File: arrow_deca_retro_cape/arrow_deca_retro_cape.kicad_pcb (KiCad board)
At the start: 4 copper layers, 73.7 x 62 mm, 23 parts, among them J1 PMOD_A, J2 P8_Male, J3 P9_Male, U1 AS4C32M16SB-7TIN, U2 AS4C32M16SB-7TIN, U3 74LVC1G04

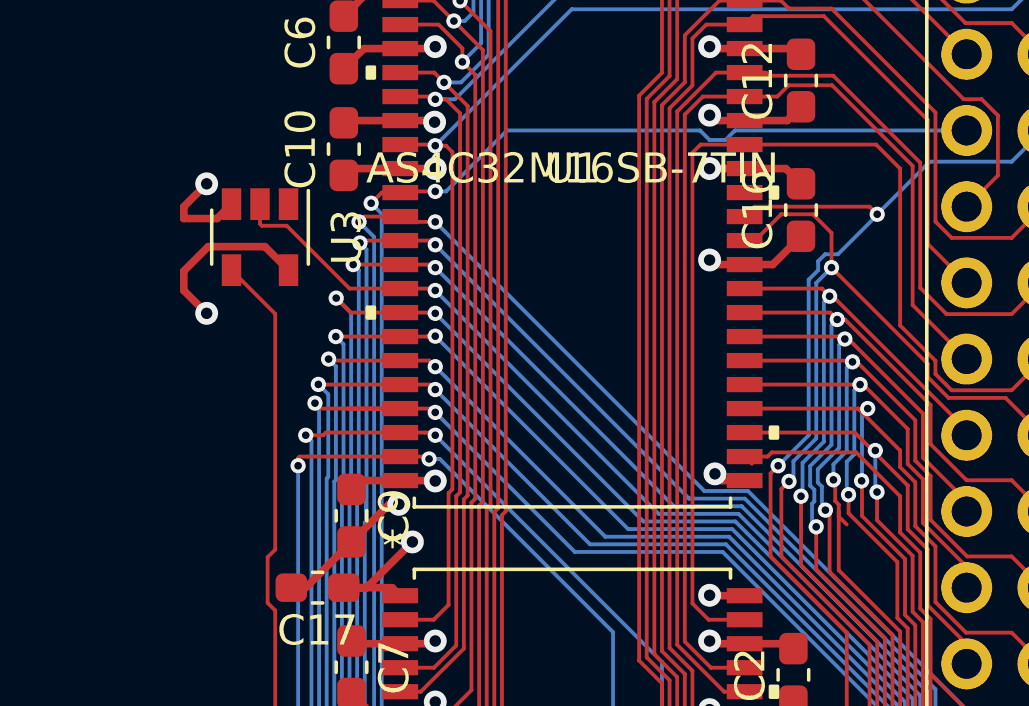
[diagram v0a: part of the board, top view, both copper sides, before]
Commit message: Starting to add VGA.
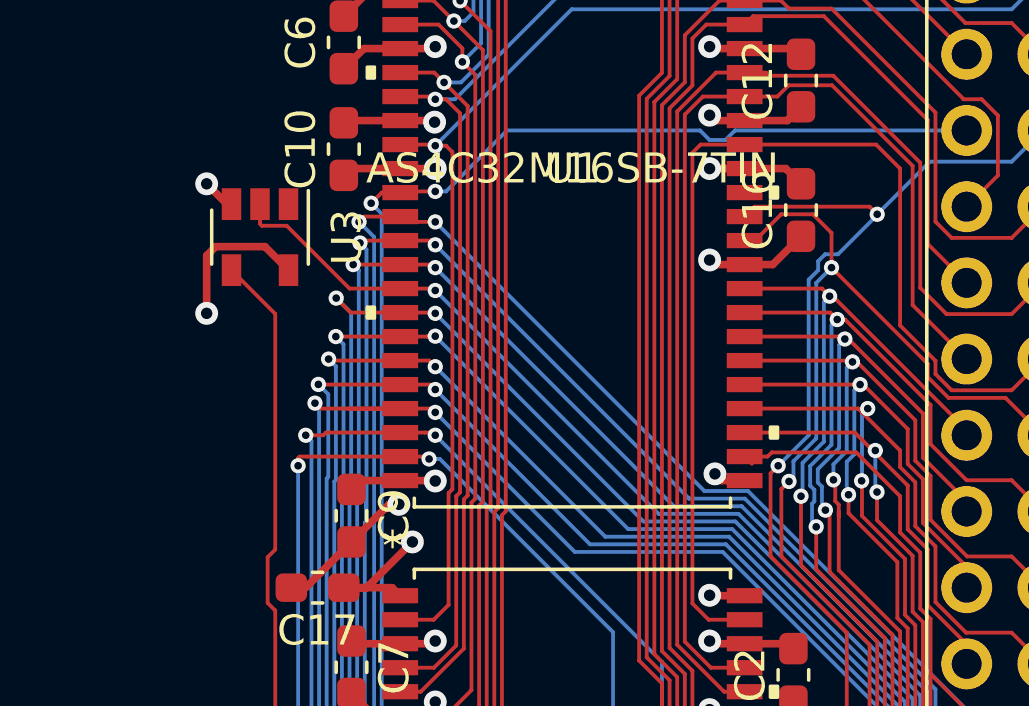
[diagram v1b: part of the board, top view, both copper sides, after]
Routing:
- net GND: track 340.9 -> 338.8 mm
- net +3V3: track 258.1 -> 257.3 mm
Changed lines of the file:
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@@
     (thickness 1.6)
     (drawings 4)
-    (tracks 1069)
+    (tracks 1065)
     (zones 0)
     (modules 23)
@@
   (segment (start 109.474 46.736) (end 109.474 55.626) (width 0.254) (layer In1.Cu) (net 1))
   (segment (start 109.474 55.626) (end 109.474 59.436) (width 0.254) (layer In1.Cu) (net 1))
-  (segment (start 96.615 48.655) (end 97.094 48.176) (width 0.254) (layer F.Cu) (net 1))
-  (segment (start 95.504 48.655) (end 96.615 48.655) (width 0.254) (layer F.Cu) (net 1))
-  (segment (start 95.504 48.26) (end 96.266 47.498) (width 0.254) (layer F.Cu) (net 1))
   (via (at 96.266 47.498) (size 0.762) (drill 0.381) (layers F.Cu B.Cu) (net 1))
-  (segment (start 95.504 48.655) (end 95.504 48.26) (width 0.254) (layer F.Cu) (net 1))
   (segment (start 109.474 46.228) (end 107.696 46.228) (width 0.254) (layer In1.Cu) (net 1))
   (segment (start 109.474 44.704) (end 109.474 46.228) (width 0.254) (layer In1.Cu) (net 1))
@@
   (segment (start 110.998 65.278) (end 110.49 64.77) (width 0.254) (layer In1.Cu) (net 1))
   (segment (start 109.474 64.77) (end 110.49 64.77) (width 0.254) (layer In1.Cu) (net 1))
+  (segment (start 96.944 48.176) (end 96.266 47.498) (width 0.254) (layer F.Cu) (net 1))
+  (segment (start 97.094 48.176) (end 96.944 48.176) (width 0.254) (layer F.Cu) (net 1))
   (segment (start 65.999557 44.679499) (end 60.706 39.385942) (width 0.127) (layer F.Cu) (net 17))
   (segment (start 67.539499 44.679499) (end 65.999557 44.679499) (width 0.127) (layer F.Cu) (net 17))
@@
   (segment (start 105.156 27.94) (end 108.712 31.496) (width 0.254) (layer In2.Cu) (net 26))
   (segment (start 102.7176 57.39) (end 101.388 57.39) (width 0.254) (layer F.Cu) (net 26))
-  (segment (start 98.209999 49.591999) (end 96.317001 49.591999) (width 0.254) (layer F.Cu) (net 26))
-  (segment (start 96.317001 49.591999) (end 95.504 50.405) (width 0.254) (layer F.Cu) (net 26))
-  (segment (start 98.994 50.376) (end 98.209999 49.591999) (width 0.254) (layer F.Cu) (net 26))
   (via (at 96.266 51.816) (size 0.762) (drill 0.381) (layers F.Cu B.Cu) (net 26))
-  (segment (start 95.504 51.054) (end 96.266 51.816) (width 0.254) (layer F.Cu) (net 26))
-  (segment (start 95.504 50.405) (end 95.504 51.054) (width 0.254) (layer F.Cu) (net 26))
   (segment (start 96.266 51.816) (end 96.266 50.038) (width 0.254) (layer In2.Cu) (net 26))
   (segment (start 99.314 46.99) (end 103.886 46.99) (width 0.254) (layer In2.Cu) (net 26))
@@
   (segment (start 105.918 59.436) (end 103.124 59.436) (width 0.254) (layer In2.Cu) (net 26))
   (segment (start 106.426 59.944) (end 105.918 59.436) (width 0.254) (layer In2.Cu) (net 26))
+  (segment (start 96.266 49.891798) (end 96.266 51.816) (width 0.254) (layer F.Cu) (net 26))
+  (segment (start 98.209999 49.591999) (end 96.565799 49.591999) (width 0.254) (layer F.Cu) (net 26))
+  (segment (start 96.565799 49.591999) (end 96.266 49.891798) (width 0.254) (layer F.Cu) (net 26))
+  (segment (start 98.994 50.376) (end 98.209999 49.591999) (width 0.254) (layer F.Cu) (net 26))
   (via (at 101.854 81.28) (size 0.508) (drill 0.254) (layers F.Cu B.Cu) (net 27))
   (segment (start 102.665599 81.28) (end 102.7176 81.227999) (width 0.127) (layer F.Cu) (net 27))
@@
   (segment (start 119.797466 61.762116) (end 119.797466 59.897015) (width 0.127) (layer F.Cu) (net 42))
   (via (at 117.158245 57.365676) (size 0.508) (drill 0.254) (layers F.Cu B.Cu) (net 43))
-  (segment (start 117.601979 58.854098) (end 117.335379 58.587498) (width 0.127) (layer F.Cu) (net 43))
   (segment (start 117.55715 75.39315) (end 117.601979 75.348321) (width 0.127) (layer F.Cu) (net 43))
   (segment (start 117.335379 58.587498) (end 117.335379 58.432621) (width 0.127) (layer F.Cu) (net 43))

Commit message: Layout finished.
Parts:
- added J4: JOY0, snapeda:TE_1-1634580-2, F.Cu at (55.2, 39.4)
- added J5: MD-60SM, MD-60SM:MD-60SM, F.Cu at (100.8, 26.4)
- added J6: JOY1, snapeda:TE_1-1634580-2, F.Cu at (55.2, 71.2)
- added R1: 1K, Resistor_SMD:R_0603_1608Metric_Pad1.05x0.95mm_HandSolder, F.Cu at (118.1, 32.9)
- added R10: 2K, Resistor_SMD:R_0603_1608Metric_Pad1.05x0.95mm_HandSolder, F.Cu at (60.4, 36.6)
- added R11: 2K, Resistor_SMD:R_0603_1608Metric_Pad1.05x0.95mm_HandSolder, F.Cu at (60.4, 33.5)
- added R12: 2K, Resistor_SMD:R_0603_1608Metric_Pad1.05x0.95mm_HandSolder, F.Cu at (60.4, 80.1)
- added R13: 2K, Resistor_SMD:R_0603_1608Metric_Pad1.05x0.95mm_HandSolder, F.Cu at (60.4, 77.1)
- added R14: 2K, Resistor_SMD:R_0603_1608Metric_Pad1.05x0.95mm_HandSolder, F.Cu at (60.4, 74.0)
- added R15: 2K, Resistor_SMD:R_0603_1608Metric_Pad1.05x0.95mm_HandSolder, F.Cu at (60.4, 71.0)
- added R16: 2K, Resistor_SMD:R_0603_1608Metric_Pad1.05x0.95mm_HandSolder, F.Cu at (60.4, 67.9)
- added R17: 2K, Resistor_SMD:R_0603_1608Metric_Pad1.05x0.95mm_HandSolder, F.Cu at (60.4, 64.9)
- added R18: 2K, Resistor_SMD:R_0603_1608Metric_Pad1.05x0.95mm_HandSolder, F.Cu at (60.4, 61.8)
- added R19: 5K, Resistor_SMD:R_0603_1608Metric_Pad1.05x0.95mm_HandSolder, F.Cu at (60.4, 50.3)
- added R2: 1K, Resistor_SMD:R_0603_1608Metric_Pad1.05x0.95mm_HandSolder, F.Cu at (118.1, 28.4)
- added R20: 5K, Resistor_SMD:R_0603_1608Metric_Pad1.05x0.95mm_HandSolder, F.Cu at (60.4, 78.6)
- added R21: 5K, Resistor_SMD:R_0603_1608Metric_Pad1.05x0.95mm_HandSolder, F.Cu at (60.4, 47.2)
- added R22: 5K, Resistor_SMD:R_0603_1608Metric_Pad1.05x0.95mm_HandSolder, F.Cu at (60.4, 75.6)
- added R23: 5K, Resistor_SMD:R_0603_1608Metric_Pad1.05x0.95mm_HandSolder, F.Cu at (60.4, 44.2)
- added R24: 5K, Resistor_SMD:R_0603_1608Metric_Pad1.05x0.95mm_HandSolder, F.Cu at (60.4, 72.5)
- added R25: 5K, Resistor_SMD:R_0603_1608Metric_Pad1.05x0.95mm_HandSolder, F.Cu at (60.4, 41.1)
- added R26: 5K, Resistor_SMD:R_0603_1608Metric_Pad1.05x0.95mm_HandSolder, F.Cu at (60.4, 69.5)
- added R27: 5K, Resistor_SMD:R_0603_1608Metric_Pad1.05x0.95mm_HandSolder, F.Cu at (60.4, 38.1)
- added R28: 5K, Resistor_SMD:R_0603_1608Metric_Pad1.05x0.95mm_HandSolder, F.Cu at (60.4, 66.4)
- added R29: 5K, Resistor_SMD:R_0603_1608Metric_Pad1.05x0.95mm_HandSolder, F.Cu at (60.4, 35.1)
- added R3: 10K, Resistor_SMD:R_0603_1608Metric_Pad1.05x0.95mm_HandSolder, F.Cu at (118.1, 31.4)
- added R30: 5K, Resistor_SMD:R_0603_1608Metric_Pad1.05x0.95mm_HandSolder, F.Cu at (60.4, 63.4)
- added R31: 5K, Resistor_SMD:R_0603_1608Metric_Pad1.05x0.95mm_HandSolder, F.Cu at (60.4, 32.0)
- added R32: 5K, Resistor_SMD:R_0603_1608Metric_Pad1.05x0.95mm_HandSolder, F.Cu at (60.4, 60.3)
- added R4: 10K, Resistor_SMD:R_0603_1608Metric_Pad1.05x0.95mm_HandSolder, F.Cu at (118.1, 29.9)
- added R5: 2K, Resistor_SMD:R_0603_1608Metric_Pad1.05x0.95mm_HandSolder, F.Cu at (60.4, 51.8)
- added R6: 2K, Resistor_SMD:R_0603_1608Metric_Pad1.05x0.95mm_HandSolder, F.Cu at (60.4, 48.8)
- added R7: 2K, Resistor_SMD:R_0603_1608Metric_Pad1.05x0.95mm_HandSolder, F.Cu at (60.4, 45.7)
- added R8: 2K, Resistor_SMD:R_0603_1608Metric_Pad1.05x0.95mm_HandSolder, F.Cu at (60.4, 42.7)
- added R9: 2K, Resistor_SMD:R_0603_1608Metric_Pad1.05x0.95mm_HandSolder, F.Cu at (60.4, 39.6)
- moved J1 28.1 mm to (87.5, 33.9), turned to 270 degrees
- moved C4 1.01 mm to (101.1, 70.5)
- moved C10 0.87 mm to (100.8, 45.5)
- moved C5 0.86 mm to (101.1, 67.1)
- moved C6 0.71 mm to (100.8, 42.1)
- moved C11 0.58 mm to (100.8, 38.7)
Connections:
- J2 pad 3: Net-(J2-Pad3) -> (no net)
- J2 pad 35: Net-(J2-Pad35) -> (no net)
- J2 pad 36: Net-(J2-Pad36) -> (no net)
- J2 pad 4: Net-(J2-Pad4) -> /PS2_CLK
- J2 pad 5: Net-(J2-Pad5) -> (no net)
- J2 pad 6: Net-(J2-Pad6) -> /PS2_DATA
- J3 pad 10: /SYS_RESET_n -> (no net)
- J3 pad 11: /GPIO1_D0 -> /GPIO1_D6
- J3 pad 12: /GPIO1_D1 -> /GPIO1_D7
- J3 pad 13: /GPIO1_D2 -> /GPIO1_D4
- J3 pad 14: /GPIO1_D3 -> /GPIO1_D5
- J3 pad 15: /GPIO1_D4 -> /GPIO1_D2
- J3 pad 16: /GPIO1_D5 -> /GPIO1_D3
- J3 pad 17: /GPIO1_D6 -> /GPIO1_D0
- J3 pad 18: /GPIO1_D7 -> /GPIO1_D1
- J3 pad 19: /GPIO1_D8 -> /J0_UP
- J3 pad 20: /GPIO1_D9 -> /J0_TRIGGER
- J3 pad 21: /GPIO1_D10 -> /J0_DOWN
- J3 pad 22: /GPIO1_D11 -> /J0_LEFT
- J3 pad 23: /GPIO1_D12 -> /J0_RIGHT
- J3 pad 24: /GPIO1_D13 -> /J0_PADDLE_A
- J3 pad 25: /GPIO1_D14 -> /J0_PADDLE_B
- J3 pad 26: /GPIO1_D15 -> /J1_UP
- J3 pad 27: /GPIO1_D16 -> /J1_TRIGGER
- J3 pad 28: /GPIO1_D17 -> /J1_DOWN
- J3 pad 29: /GPIO1_D18 -> /J1_LEFT
- J3 pad 30: /GPIO1_D19 -> /J1_RIGHT
- J3 pad 31: /GPIO1_D20 -> /J1_PADDLE_A
- J3 pad 32: +1V8 -> (no net)
- J3 pad 33: /AIN6 -> (no net)
- J3 pad 34: GNDA -> (no net)
- J3 pad 35: /AIN4 -> (no net)
- J3 pad 36: /AIN5 -> (no net)
- J3 pad 37: /AIN2 -> (no net)
- J3 pad 38: /AIN3 -> (no net)
- J3 pad 39: /AIN0 -> (no net)
- J3 pad 40: /AIN1 -> (no net)
- J3 pad 41: /GPIO1_D21 -> /J1_PADDLE_B
- J3 pad 42: /GPIO1_D22 -> (no net)
- J3 pad 9: /PWR_BUT -> (no net)
- U1 pad 40: Net-(U1-Pad40) -> (no net)
- U2 pad 40: Net-(U2-Pad40) -> (no net)
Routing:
- net +5V: track 7.62 -> 87.0 mm
- net GND: track 338.8 -> 414.8 mm
- net /PS2_DATA_5V: track 0.00 -> 22.5 mm
- net /J0_TRIGGER: track 0.00 -> 20.8 mm
- net /J0_UP: track 0.00 -> 19.3 mm
- net /J1_RIGHT: track 0.00 -> 17.9 mm
- net /PS2_CLK_5V: track 0.00 -> 17.8 mm
- net /J0_LEFT: track 0.00 -> 17.5 mm
- net /J0_DOWN: track 0.00 -> 16.2 mm
- net /J1_PADDLE_A: track 0.00 -> 15.5 mm
- net /J1_DOWN: track 0.00 -> 14.0 mm
- net /J0_PADDLE_A: track 0.00 -> 13.3 mm
- net /J1_LEFT: track 0.00 -> 13.0 mm
- net /J0_RIGHT: track 0.00 -> 12.2 mm
- net /J1_UP: track 0.00 -> 11.6 mm
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- added copper zone on In2.Cu, net +3V3
- added copper zone on B.Cu, net +5V
- added copper zone on B.Cu, net GND
- added copper zone on F.Cu, net GND
- added copper zone on In1.Cu, net GND
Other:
- board size 73.7 x 62 mm -> 75.8 x 64.5 mm
- board text added: "Arrow DECA Retro Cape Tom Verbeure https://github.com/tomverbeure/arrow_deca_retro_cape"
- board text added: "Joy 0"
- board text added: "Joy 1"
- board text added: "PMOD"
- board text added: "PS/2 Keyboard Only!"

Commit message: rev1, sent to JLPCB.
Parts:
- added C18: 10uF, Capacitor_SMD:C_0805_2012Metric_Pad1.15x1.40mm_HandSolder, F.Cu at (73.4, 48.0)
- added C19: 100uF, Capacitor_SMD:C_0805_2012Metric_Pad1.15x1.40mm_HandSolder, F.Cu at (84.3, 45.8)
- added J7: Conn_01x03, Connector_PinHeader_2.54mm:PinHeader_1x03_P2.54mm_Vertical, F.Cu at (87.2, 44.3)
- added J8: Conn_01x06, Connector_PinHeader_2.54mm:PinHeader_1x06_P2.54mm_Vertical, F.Cu at (96.4, 65.7)
- added U4: LM1117-3.3, Package_TO_SOT_SMD:SOT-223-3_TabPin2, F.Cu at (78.8, 46.6)
- J1: value PMOD_A -> PMOD
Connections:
- net /GPIO1_D0 renamed /PMOD_D0
- net /GPIO1_D1 renamed /PMOD_D1
- net /GPIO1_D2 renamed /PMOD_D2
- net /GPIO1_D3 renamed /PMOD_D3
- net /GPIO1_D4 renamed /PMOD_D4
- net /GPIO1_D5 renamed /PMOD_D5
- net /GPIO1_D6 renamed /PMOD_D6
- net /GPIO1_D7 renamed /PMOD_D7
- J2 pad 3: (no net) -> /GPIO0
- J2 pad 35: (no net) -> /GPIO2
- J2 pad 36: (no net) -> /GPIO3
- J2 pad 5: (no net) -> /GPIO1
- J3 pad 3: +3V3 -> +3.3VP
- J3 pad 4: +3V3 -> +3.3VP
- J3 pad 41: /J1_PADDLE_B -> (no net)
- J3 pad 42: (no net) -> /J1_PADDLE_B
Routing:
- net /GPIO1: track 0.00 -> 61.9 mm
- net /GPIO0: track 0.00 -> 59.4 mm
- net /GPIO3: track 0.00 -> 46.9 mm
- net /GPIO2: track 0.00 -> 46.0 mm
- net GND: track 414.8 -> 459.6 mm, vias 17 -> 19
- net +3.3VP: track 0.00 -> 32.0 mm
- net +5V: track 87.0 -> 108.1 mm, vias 0 -> 1
- net /3V3_LDO: track 0.00 -> 13.3 mm
- net +3V3: track 263.7 -> 256.0 mm
- net /J1_TRIGGER: track 8.67 -> 11.7 mm
- net /J1_PADDLE_B: track 7.25 -> 9.79 mm
- net /PMOD_D6: track 11.6 -> 13.8 mm
- net /J1_PADDLE_A: track 15.5 -> 17.7 mm
- net /J1_DOWN: track 14.0 -> 15.7 mm
- net /J1_LEFT: track 13.0 -> 14.3 mm
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- added copper zone on In2.Cu, net +3.3VP
- removed copper zone on B.Cu, net GND
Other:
- outline, holes or cut-outs redrawn
- board text added: "3V3"
- board text added: "3V3_LDO"
